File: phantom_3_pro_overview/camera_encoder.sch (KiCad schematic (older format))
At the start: 7 parts

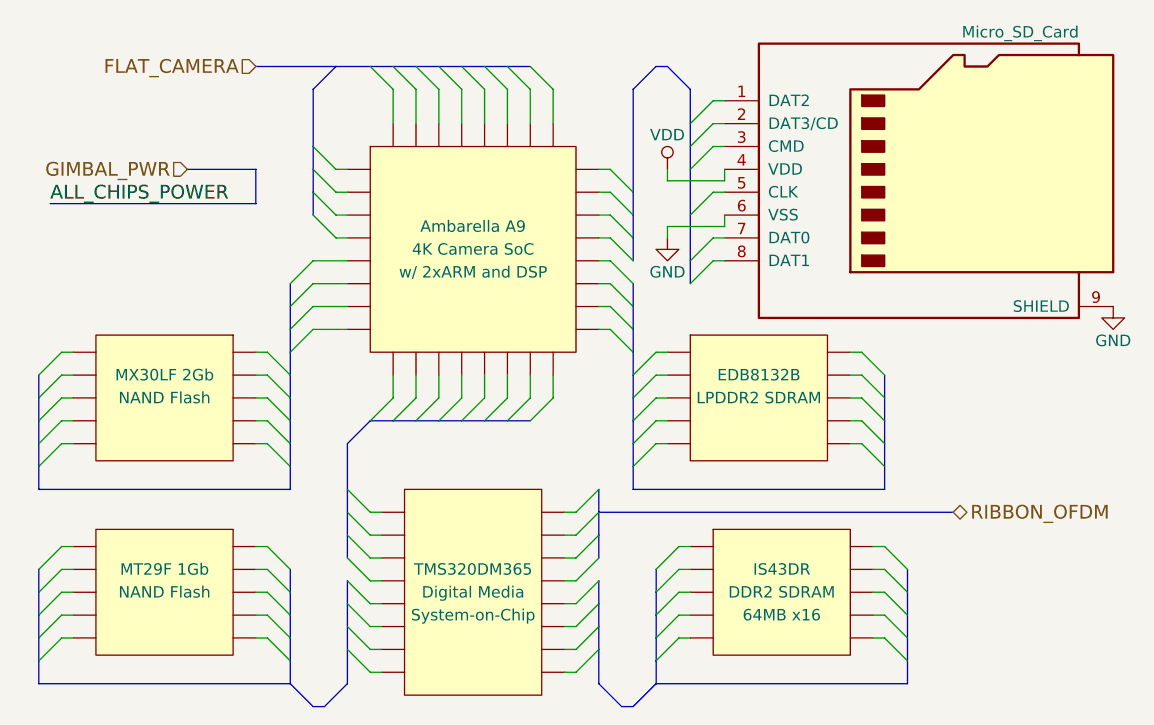
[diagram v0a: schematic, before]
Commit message: Overview: Updated encoder to include micro-USB.
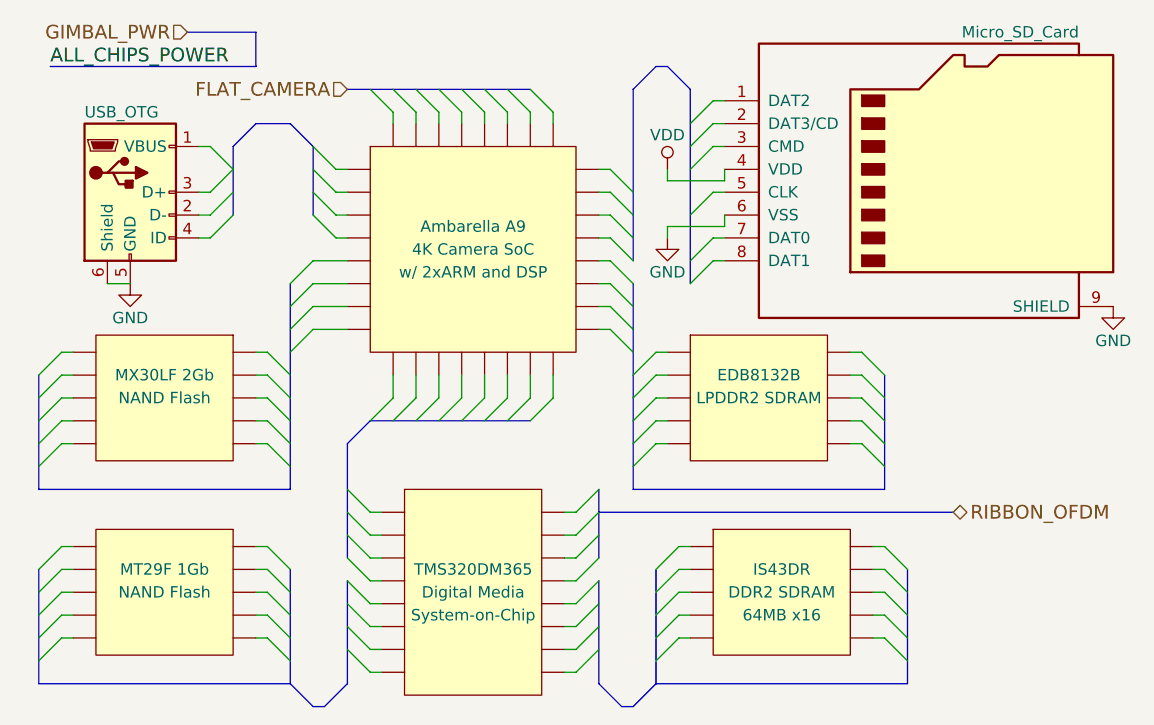
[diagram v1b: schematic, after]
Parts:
- added J?: USB_OTG, symbol USB_OTG
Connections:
- net GND: now also J?.5 (GND), J?.6 (Shield)

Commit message: Overview: Upgraded to KiCAD 5.0.1.
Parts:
- J?: symbol Micro_SD_Card -> Connector:Micro_SD_Card
- J?: symbol USB_OTG -> Connector:USB_OTG
- U?: symbol IC_PQFP32 -> ic_dil_generic:IC_PQFP32
- U?: symbol IC_DIL16 -> ic_dil_generic:IC_DIL16
- U? (x4): symbol IC_DIL10 -> ic_dil_generic:IC_DIL10
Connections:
- net GND: no longer J?.6 (Shield)
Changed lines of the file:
@@
-EESchema Schematic File Version 2
-LIBS:power
-LIBS:device
-LIBS:transistors
-LIBS:conn
-LIBS:linear
-LIBS:regul
-LIBS:74xx
-LIBS:cmos4000
-LIBS:adc-dac
-LIBS:memory
-LIBS:xilinx
-LIBS:microcontrollers
-LIBS:dsp
-LIBS:microchip
-LIBS:analog_switches
-LIBS:motorola
-LIBS:texas
-LIBS:intel
-LIBS:audio
-LIBS:interface
-LIBS:digital-audio
-LIBS:philips
-LIBS:display
-LIBS:cypress
-LIBS:siliconi
-LIBS:opto
-LIBS:atmel
-LIBS:contrib
-LIBS:valves
-LIBS:motors
-LIBS:ic_dil_generic
-LIBS:sensors
-LIBS:u-blox
-LIBS:amplifiers
-LIBS:transistors-switches
-LIBS:transistors-power
-LIBS:sensors-v2
-LIBS:regul-v2
+EESchema Schematic File Version 4
 LIBS:phantom_3_pro_overview-cache
-EELAYER 25 0
+EELAYER 26 0
 EELAYER END
 $Descr User 5906 5315
@@
 FLAT_CAMERA
 $Comp
-L IC_PQFP32 U?
+L ic_dil_generic:IC_PQFP32 U?
 U 1 1 597C8092
 P 2450 1500
@@
 $EndComp
 $Comp
-L Micro_SD_Card J?
+L Connector:Micro_SD_Card J?
 U 1 1 597C8098
 P 4450 1150
@@
 $EndComp
 $Comp
-L GND #PWR?
+L power:GND #PWR?
 U 1 1 597C809E
 P 5250 1750
@@
 	1850 1150 1750 1050
 $Comp
-L VDD #PWR?
+L power:VDD #PWR?
 U 1 1 597C80CC
 P 3300 1150
@@
 $EndComp
 $Comp
-L GND #PWR?
+L power:GND #PWR?
 U 1 1 597C80D2
 P 3300 1450
@@
 $EndComp
 $Comp
-L IC_DIL16 U?
+L ic_dil_generic:IC_DIL16 U?
 U 1 1 597C810B
 P 2450 3000
@@
 	2900 2650 3000 2550
 $Comp
-L IC_DIL10 U?
+L ic_dil_generic:IC_DIL10 U?
 U 1 1 597C8C07
 P 3800 3000
@@
 	3250 2900 3350 2800
 $Comp
-L IC_DIL10 U?
+L ic_dil_generic:IC_DIL10 U?
 U 1 1 597C8ED7
 P 1100 3000
@@
 	1650 2900 1550 2800
 $Comp
-L IC_DIL10 U?
+L ic_dil_generic:IC_DIL10 U?
 U 1 1 597C8FED
 P 3700 2150
@@
 	3150 2050 3250 1950
 $Comp
-L IC_DIL10 U?
+L ic_dil_generic:IC_DIL10 U?
 U 1 1 597C926F
 P 1100 2150
@@
 	1750 1850 1900 1850
 Wire Bus Line
-	3400 800  3400 1650
-Wire Bus Line
-	1900 800  2700 800
-Wire Bus Line
 	3250 700  3300 700
 Wire Wire Line
@@
 Wire Wire Line
 	3300 1400 3300 1450
-Wire Bus Line
-	1900 2350 1900 2850
 Wire Wire Line
 	2000 2650 2050 2650
@@
 	2900 2650 2850 2650
 Wire Bus Line
-	3250 2900 3250 3400
-Wire Bus Line
 	3100 3500 3150 3500
 Wire Wire Line
@@
 	3400 3200 3350 3200
 Wire Bus Line
-	4350 2900 4350 3400
-Wire Bus Line
 	4350 3400 3250 3400
 Wire Bus Line
-	3000 2550 3000 2850
-Wire Bus Line
-	3000 2950 3000 3400
-Wire Bus Line
-	1650 2900 1650 3400
+	3000 2550 3000 2650
 Wire Bus Line
 	1800 3500 1750 3500
@@
 	1500 3200 1550 3200
 Wire Bus Line
-	550  2900 550  3400
-Wire Bus Line
 	550  3400 1650 3400
-Wire Bus Line
-	1900 2950 1900 3400
-Wire Bus Line
-	3150 1650 3150 2550
 Wire Wire Line
 	4100 1950 4150 1950
@@
 	3300 2350 3250 2350
 Wire Bus Line
-	4250 2050 4250 2550
-Wire Bus Line
 	4250 2550 3150 2550
 Wire Bus Line
-	3150 800  3150 1550
-Wire Bus Line
 	3000 2650 4550 2650
-Wire Bus Line
-	1650 1650 1650 2550
 Wire Wire Line
 	700  1950 650  1950
@@
 	1500 2350 1550 2350
 Wire Bus Line
-	550  2050 550  2550
-Wire Bus Line
 	550  2550 1650 2550
-Wire Bus Line
-	2000 2250 2700 2250
 Wire Bus Line
 	1500 700  600  700
@@
 	1500 550  1500 700
 $Comp
-L USB_OTG J?
+L Connector:USB_OTG J?
 U 1 1 5A25C2C9
 P 950 1250
@@
 Wire Wire Line
 	1250 1050 1300 1050
-Wire Bus Line
-	1750 1050 1750 1350
 Entry Bus Bus
 	1400 1050 1500 950
@@
 	1650 950  1500 950
 $Comp
-L GND #PWR?
+L power:GND #PWR?
 U 1 1 5A25CB22
 P 950 1650
@@
 	1    0    0    -1
 $EndComp
-Wire Wire Line
-	850  1650 950  1650
-Wire Bus Line
-	1400 1350 1400 1050
+Wire Bus Line
+	1750 1050 1750 1350
+Wire Bus Line
+	3000 2650 3000 2850
+Wire Bus Line
+	1400 1050 1400 1350
+Wire Bus Line
+	1900 2350 1900 2850
+Wire Bus Line
+	3000 2950 3000 3400
+Wire Bus Line
+	1900 2950 1900 3400
+Wire Bus Line
+	3150 800  3150 1550
+Wire Bus Line
+	3400 800  3400 1650
+Wire Bus Line
+	2000 2250 2700 2250
+Wire Bus Line
+	4350 2900 4350 3400
+Wire Bus Line
+	3250 2900 3250 3400
+Wire Bus Line
+	550  2900 550  3400
+Wire Bus Line
+	1650 2900 1650 3400
+Wire Bus Line
+	4250 2050 4250 2550
+Wire Bus Line
+	550  2050 550  2550
+Wire Bus Line
+	1900 800  2700 800
+Wire Bus Line
+	3150 1650 3150 2550
+Wire Bus Line
+	1650 1650 1650 2550
 $EndSCHEMATC
